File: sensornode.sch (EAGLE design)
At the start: 73 parts, among them IC1 CP2104, Q1 mmbt2222, Q2 mmbt2222, Q3 DMG3415U, SW2 KMR2, U1 TSL2591, U2 AP2112-3.3, U3 MCP73831T-2ACI/OT, U4 BMEx80, X2 ESP32_WROOM32_SKINNY, X4 20329

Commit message: Adding a 10uF Cap to the CP2104
This make it more closely resemble the known working designs.
Getting paranoid due to when this will need to get built.
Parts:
- added C5: 10uF, microbuilder:CAP_CERAMIC0805-NOOUTLINE
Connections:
- new net N$6: C5.2, IC1G$1.VDD
- net GND: now also C5.1
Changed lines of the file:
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@@
 <part name="U$31" library="microbuilder" deviceset="GND" device=""/>
 <part name="U$45" library="microbuilder" deviceset="3.3V" device=""/>
+<part name="C5" library="microbuilder" deviceset="CAP_CERAMIC" device="0805-NOOUTLINE" value="10uF"/>
+<part name="U$46" library="microbuilder" deviceset="GND" device=""/>
 </parts>
 <sheets>
@@
 <instance part="U$31" gate="G$1" x="292.1" y="5.08"/>
 <instance part="U$45" gate="G$1" x="276.86" y="63.5"/>
+<instance part="C5" gate="G$1" x="177.8" y="248.92"/>
+<instance part="U$46" gate="G$1" x="177.8" y="259.08" rot="R180"/>
 </instances>
 <busses>
@@
 <junction x="292.1" y="48.26"/>
 </segment>
+<segment>
+<pinref part="C5" gate="G$1" pin="1"/>
+<pinref part="U$46" gate="G$1" pin="GND"/>
+<wire x1="177.8" y1="254" x2="177.8" y2="256.54" width="0.1524" layer="91"/>
+</segment>
 </net>
 <net name="TXLED" class="0">
@@
 </segment>
 </net>
+<net name="N$6" class="0">
+<segment>
+<pinref part="IC1" gate="G$1" pin="VDD"/>
+<pinref part="C5" gate="G$1" pin="2"/>
+<wire x1="195.58" y1="243.84" x2="177.8" y2="243.84" width="0.1524" layer="91"/>
+<wire x1="177.8" y1="243.84" x2="177.8" y2="246.38" width="0.1524" layer="91"/>
+</segment>
+</net>

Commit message: Cleaning up a bunch of stuff
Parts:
- added JP1: (no value), pinhead:PINHD-1X6
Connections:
- net GND: now also JP1.1
- net RXD0: now also JP1.5
- net TXD0: now also JP1.4
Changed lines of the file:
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@@
 <part name="C5" library="microbuilder" deviceset="CAP_CERAMIC" device="0805-NOOUTLINE" value="10uF"/>
 <part name="U$46" library="microbuilder" deviceset="GND" device=""/>
+<part name="JP1" library="pinhead" deviceset="PINHD-1X6" device=""/>
 </parts>
 <sheets>
@@
 <instance part="C5" gate="G$1" x="177.8" y="248.92"/>
 <instance part="U$46" gate="G$1" x="177.8" y="259.08" rot="R180"/>
+<instance part="JP1" gate="A" x="274.32" y="165.1"/>
 </instances>
 <busses>
@@
 <wire x1="177.8" y1="254" x2="177.8" y2="256.54" width="0.1524" layer="91"/>
 </segment>
+<segment>
+<pinref part="JP1" gate="A" pin="1"/>
+<wire x1="271.78" y1="172.72" x2="254" y2="172.72" width="0.1524" layer="91"/>
+<label x="256.54" y="172.72" size="1.778" layer="95"/>
+</segment>
 </net>
 <net name="TXLED" class="0">
@@
 <label x="228.6" y="210.82" size="1.778" layer="95"/>
 </segment>
+<segment>
+<pinref part="JP1" gate="A" pin="5"/>
+<wire x1="271.78" y1="162.56" x2="254" y2="162.56" width="0.1524" layer="91"/>
+<label x="256.54" y="162.56" size="1.778" layer="95"/>
+</segment>
 </net>
 <net name="TXD0" class="0">
@@
 <label x="228.6" y="208.28" size="1.778" layer="95"/>
 </segment>
-</net>
+<segment>
+<pinref part="JP1" gate="A" pin="4"/>
+<wire x1="271.78" y1="165.1" x2="254" y2="165.1" width="0.1524" layer="91"/>
+<label x="256.54" y="165.1" size="1.778" layer="95"/>
+</segment>
+</net>

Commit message: Final cleanups going to prototype v2
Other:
- note added: "BACKUP FTDI Port"
- note added: "E-Ink Screen Connector"
- note added: "Micro SD Card Cage"
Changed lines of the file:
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@@
 <wire x1="71.12" y1="50.8" x2="71.12" y2="124.46" width="0.1524" layer="94" style="shortdash"/>
 <wire x1="251.46" y1="187.96" x2="284.48" y2="187.96" width="0.1524" layer="94" style="shortdash"/>
-<wire x1="251.46" y1="63.5" x2="251.46" y2="144.78" width="0.1524" layer="94" style="shortdash"/>
+<wire x1="251.46" y1="63.5" x2="251.46" y2="71.12" width="0.1524" layer="94" style="shortdash"/>
+<wire x1="251.46" y1="71.12" x2="251.46" y2="144.78" width="0.1524" layer="94" style="shortdash"/>
 <wire x1="251.46" y1="144.78" x2="251.46" y2="187.96" width="0.1524" layer="94" style="shortdash"/>
 <wire x1="251.46" y1="63.5" x2="236.22" y2="63.5" width="0.1524" layer="94" style="shortdash"/>
@@
 <text x="289.56" y="147.32" size="1.778" layer="97">BME280 - Temp, Humidity, Pressure
 BME680 - Temp, Humidity, Pressure, Particle</text>
-<wire x1="284.48" y1="71.12" x2="284.48" y2="162.56" width="0.1524" layer="94" style="shortdash"/>
-<wire x1="401.32" y1="71.12" x2="284.48" y2="71.12" width="0.1524" layer="94" style="shortdash"/>
+<wire x1="284.48" y1="71.12" x2="284.48" y2="144.78" width="0.1524" layer="94" style="shortdash"/>
+<wire x1="284.48" y1="144.78" x2="284.48" y2="162.56" width="0.1524" layer="94" style="shortdash"/>
+<wire x1="401.32" y1="71.12" x2="299.72" y2="71.12" width="0.1524" layer="94" style="shortdash"/>
+<text x="254" y="182.88" size="1.778" layer="94">BACKUP FTDI Port</text>
+<text x="149.86" y="139.7" size="1.778" layer="94">E-Ink Screen Connector</text>
+<wire x1="299.72" y1="71.12" x2="284.48" y2="71.12" width="0.1524" layer="94" style="shortdash"/>
+<wire x1="251.46" y1="144.78" x2="284.48" y2="144.78" width="0.1524" layer="94" style="shortdash"/>
+<text x="254" y="68.58" size="1.778" layer="94">Micro SD Card Cage</text>
+<wire x1="251.46" y1="71.12" x2="284.48" y2="71.12" width="0.1524" layer="94" style="shortdash"/>
+<wire x1="299.72" y1="22.86" x2="299.72" y2="71.12" width="0.1524" layer="94" style="shortdash"/>
 </plain>
 <instances>

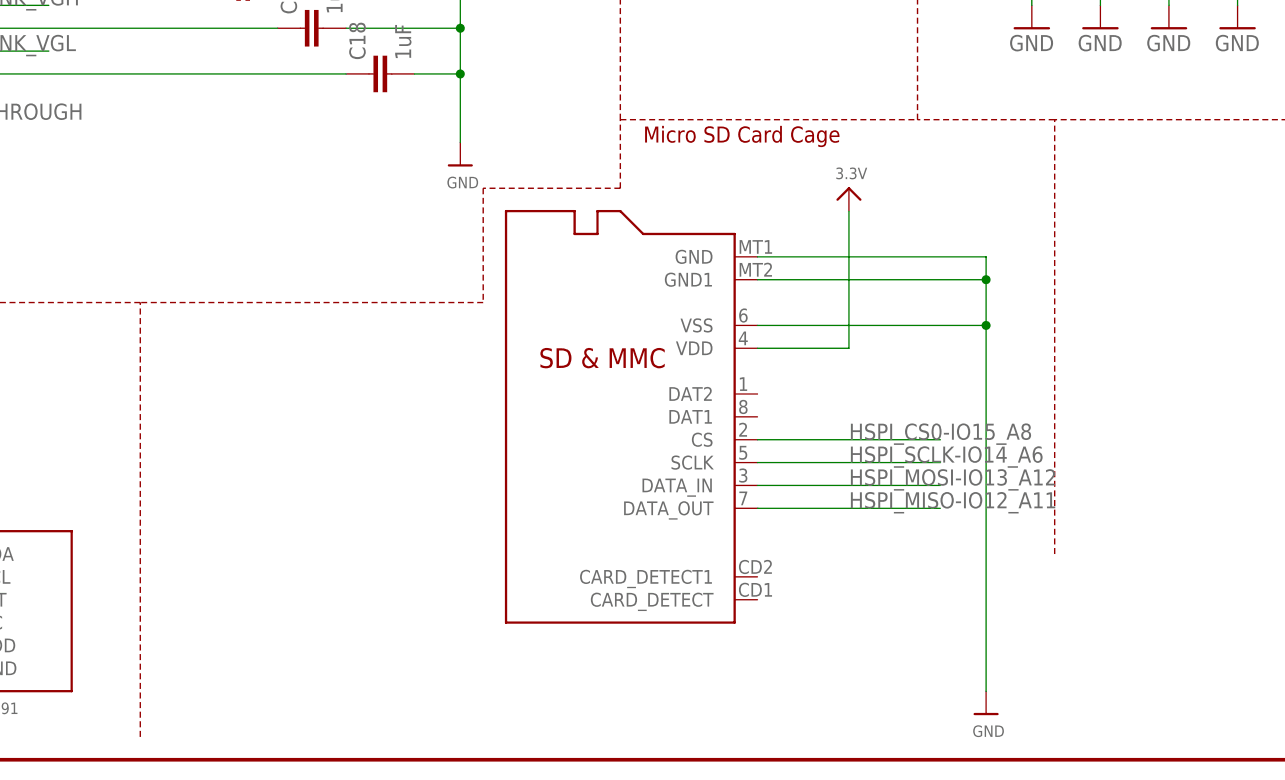
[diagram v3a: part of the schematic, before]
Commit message: Swapping out microSD cage for the Molex
The 4UConn cage is delightlyfully cheap, but the lead times are
dicey.  At least for this run I'm going to go with the easily
found, but more expensive, card cage, and I'll revert when
I've got more time on a different production run.
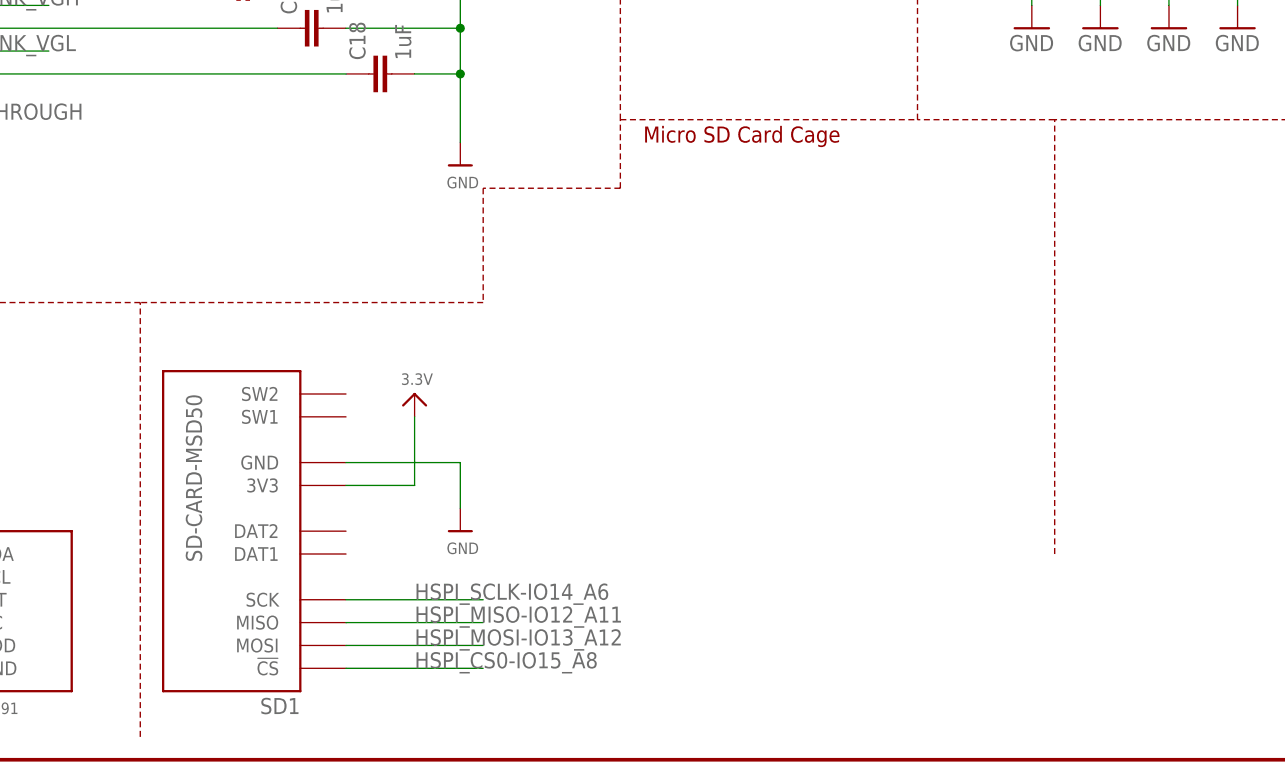
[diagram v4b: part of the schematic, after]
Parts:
- removed U$17: MICROSD, adafruit:MICROSD
- added SD1: SD-CARD-MSD50, we-con:SD-CARD-MSD50
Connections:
- net 3.3V: now also SD1.3V3; no longer U$17.VDD
- net GND: now also SD1.GND; no longer U$17.GND, U$17.GND1, U$17.VSS
- net HSPI_CS0-IO15_A8: now also SD1.!CS; no longer U$17.CS
- net HSPI_MISO-IO12_A11: now also SD1.MISO; no longer U$17.DATA_OUT
- net HSPI_MOSI-IO13_A12: now also SD1.MOSI; no longer U$17.DATA_IN
- net HSPI_SCLK-IO14_A6: now also SD1.SCK; no longer U$17.SCLK
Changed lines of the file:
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@@
 <part name="U$47" library="microbuilder" deviceset="GND" device=""/>
 <part name="U$18" library="microbuilder" deviceset="VBUS" device=""/>
-<part name="U$17" library="adafruit" deviceset="MICROSD" device=""/>
-<part name="U$31" library="microbuilder" deviceset="GND" device=""/>
-<part name="U$45" library="microbuilder" deviceset="3.3V" device=""/>
 <part name="C5" library="microbuilder" deviceset="CAP_CERAMIC" device="0805-NOOUTLINE" value="10uF"/>
 <part name="U$46" library="microbuilder" deviceset="GND" device=""/>
 <part name="JP1" library="pinhead" deviceset="PINHD-1X6" device=""/>
+<part name="SD1" library="we-con" deviceset="SD-CARD" device="-MSD50"/>
+<part name="U$48" library="microbuilder" deviceset="3.3V" device=""/>
+<part name="U$49" library="microbuilder" deviceset="GND" device=""/>
 </parts>
 <sheets>
@@
 <instance part="U$47" gate="G$1" x="177.8" y="226.06"/>
 <instance part="U$18" gate="G$1" x="167.64" y="259.08"/>
-<instance part="U$17" gate="G$1" x="248.92" y="35.56" rot="R180"/>
-<instance part="U$31" gate="G$1" x="292.1" y="5.08"/>
-<instance part="U$45" gate="G$1" x="276.86" y="63.5"/>
 <instance part="C5" gate="G$1" x="177.8" y="248.92"/>
 <instance part="U$46" gate="G$1" x="177.8" y="259.08" rot="R180"/>
 <instance part="JP1" gate="A" x="274.32" y="165.1"/>
+<instance part="SD1" gate="SD" x="208.28" y="25.4" rot="R180"/>
+<instance part="U$48" gate="G$1" x="228.6" y="40.64"/>
+<instance part="U$49" gate="G$1" x="233.68" y="25.4"/>
 </instances>
 <busses>
@@
 </segment>
 <segment>
-<pinref part="U$17" gate="G$1" pin="GND"/>
-<wire x1="266.7" y1="55.88" x2="292.1" y2="55.88" width="0.1524" layer="91"/>
-<wire x1="292.1" y1="55.88" x2="292.1" y2="53.34" width="0.1524" layer="91"/>
-<pinref part="U$31" gate="G$1" pin="GND"/>
-<pinref part="U$17" gate="G$1" pin="GND1"/>
-<wire x1="292.1" y1="53.34" x2="292.1" y2="48.26" width="0.1524" layer="91"/>
-<wire x1="292.1" y1="48.26" x2="292.1" y2="7.62" width="0.1524" layer="91"/>
-<wire x1="266.7" y1="53.34" x2="292.1" y2="53.34" width="0.1524" layer="91"/>
-<junction x="292.1" y="53.34"/>
-<pinref part="U$17" gate="G$1" pin="VSS"/>
-<wire x1="266.7" y1="48.26" x2="292.1" y2="48.26" width="0.1524" layer="91"/>
-<junction x="292.1" y="48.26"/>
-</segment>
-<segment>
 <pinref part="C5" gate="G$1" pin="1"/>
 <pinref part="U$46" gate="G$1" pin="GND"/>
@@
 <wire x1="271.78" y1="172.72" x2="254" y2="172.72" width="0.1524" layer="91"/>
 <label x="256.54" y="172.72" size="1.778" layer="95"/>
+</segment>
+<segment>
+<pinref part="SD1" gate="SD" pin="GND"/>
+<pinref part="U$49" gate="G$1" pin="GND"/>
+<wire x1="220.98" y1="33.02" x2="233.68" y2="33.02" width="0.1524" layer="91"/>
+<wire x1="233.68" y1="33.02" x2="233.68" y2="27.94" width="0.1524" layer="91"/>
 </segment>
 </net>
@@
 </segment>
 <segment>
-<pinref part="U$17" gate="G$1" pin="VDD"/>
-<pinref part="U$45" gate="G$1" pin="3.3V"/>
-<wire x1="266.7" y1="45.72" x2="276.86" y2="45.72" width="0.1524" layer="91"/>
-<wire x1="276.86" y1="45.72" x2="276.86" y2="60.96" width="0.1524" layer="91"/>
+<pinref part="SD1" gate="SD" pin="3V3"/>
+<pinref part="U$48" gate="G$1" pin="3.3V"/>
+<wire x1="220.98" y1="30.48" x2="228.6" y2="30.48" width="0.1524" layer="91"/>
+<wire x1="228.6" y1="30.48" x2="228.6" y2="38.1" width="0.1524" layer="91"/>
 </segment>
 </net>
@@
 </segment>
 <segment>
-<pinref part="U$17" gate="G$1" pin="DATA_IN"/>
-<wire x1="266.7" y1="30.48" x2="287.02" y2="30.48" width="0.1524" layer="91"/>
-<label x="276.86" y="30.48" size="1.778" layer="95"/>
+<pinref part="SD1" gate="SD" pin="MOSI"/>
+<wire x1="220.98" y1="12.7" x2="236.22" y2="12.7" width="0.1524" layer="91"/>
+<label x="228.6" y="12.7" size="1.778" layer="95"/>
 </segment>
 </net>
@@
 </segment>
 <segment>
-<pinref part="U$17" gate="G$1" pin="DATA_OUT"/>
-<wire x1="266.7" y1="27.94" x2="287.02" y2="27.94" width="0.1524" layer="91"/>
-<label x="276.86" y="27.94" size="1.778" layer="95"/>
+<pinref part="SD1" gate="SD" pin="MISO"/>
+<wire x1="220.98" y1="15.24" x2="236.22" y2="15.24" width="0.1524" layer="91"/>
+<label x="228.6" y="15.24" size="1.778" layer="95"/>
 </segment>
 </net>
@@
 </segment>
 <segment>
-<pinref part="U$17" gate="G$1" pin="CS"/>
-<wire x1="266.7" y1="35.56" x2="287.02" y2="35.56" width="0.1524" layer="91"/>
-<label x="276.86" y="35.56" size="1.778" layer="95"/>
+<pinref part="SD1" gate="SD" pin="!CS"/>
+<wire x1="220.98" y1="10.16" x2="236.22" y2="10.16" width="0.1524" layer="91"/>
+<label x="228.6" y="10.16" size="1.778" layer="95"/>
 </segment>
 </net>
@@
 </segment>
 <segment>
-<pinref part="U$17" gate="G$1" pin="SCLK"/>
-<wire x1="266.7" y1="33.02" x2="287.02" y2="33.02" width="0.1524" layer="91"/>
-<label x="276.86" y="33.02" size="1.778" layer="95"/>
-</segment>
-</net>
+<pinref part="SD1" gate="SD" pin="SCK"/>
+<wire x1="220.98" y1="17.78" x2="236.22" y2="17.78" width="0.1524" layer="91"/>
+<label x="228.6" y="17.78" size="1.778" layer="95"/>
+</segment>
+</net>

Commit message: Adjusting e-ink screen, and reving to v1.2
So this adds C22, a 1uF cap on VGL and R20 to EINK_GDR.  These
fall in line with what's on the waveshare and Open Hardware Summit
badge and should be slightly more reliable than my current circuit
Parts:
- added C22: 1uF, SparkFun-Capacitors:0.1UF-25V-5%(0603)
- added R20: 10K, SparkFun-Resistors:4.7KOHM-1/10W-1%(0603)
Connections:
- new net N$24: C22.1, U$15.4-NC2
- net EINK_GDR: now also R20.1
- net GND: now also C22.2, R20.2
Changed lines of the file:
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@@
 <part name="U$48" library="microbuilder" deviceset="3.3V" device=""/>
 <part name="U$49" library="microbuilder" deviceset="GND" device=""/>
+<part name="R20" library="SparkFun-Resistors" deviceset="4.7KOHM-1/10W-1%(0603)" device="" value="10K"/>
+<part name="C22" library="SparkFun-Capacitors" deviceset="0.1UF-25V-5%(0603)" device="" value="1uF"/>
 </parts>
 <sheets>
@@
 <instance part="U$48" gate="G$1" x="228.6" y="40.64"/>
 <instance part="U$49" gate="G$1" x="233.68" y="25.4"/>
+<instance part="R20" gate="G$1" x="198.12" y="137.16"/>
+<instance part="C22" gate="G$1" x="205.74" y="127" rot="R90"/>
 </instances>
 <busses>
@@
 <wire x1="228.6" y1="76.2" x2="233.68" y2="76.2" width="0.1524" layer="91"/>
 <junction x="233.68" y="76.2"/>
+<pinref part="R20" gate="G$1" pin="2"/>
+<wire x1="203.2" y1="137.16" x2="233.68" y2="137.16" width="0.1524" layer="91"/>
+<wire x1="233.68" y1="137.16" x2="233.68" y2="127" width="0.1524" layer="91"/>
+<junction x="233.68" y="124.46"/>
+<pinref part="C22" gate="G$1" pin="2"/>
+<wire x1="233.68" y1="127" x2="233.68" y2="124.46" width="0.1524" layer="91"/>
+<wire x1="208.28" y1="127" x2="233.68" y2="127" width="0.1524" layer="91"/>
+<junction x="233.68" y="127"/>
 </segment>
 <segment>
@@
 <segment>
 <pinref part="U$15" gate="G$1" pin="2-GDR"/>
-<wire x1="162.56" y1="132.08" x2="187.96" y2="132.08" width="0.1524" layer="91"/>
+<wire x1="162.56" y1="132.08" x2="177.8" y2="132.08" width="0.1524" layer="91"/>
 <label x="180.34" y="132.08" size="1.778" layer="95"/>
+<pinref part="R20" gate="G$1" pin="1"/>
+<wire x1="177.8" y1="132.08" x2="187.96" y2="132.08" width="0.1524" layer="91"/>
+<wire x1="177.8" y1="132.08" x2="177.8" y2="137.16" width="0.1524" layer="91"/>
+<wire x1="177.8" y1="137.16" x2="193.04" y2="137.16" width="0.1524" layer="91"/>
+<junction x="177.8" y="132.08"/>
 </segment>
 </net>
@@
 </segment>
 </net>
+<net name="N$24" class="0">
+<segment>
+<pinref part="U$15" gate="G$1" pin="4-NC2"/>
+<pinref part="C22" gate="G$1" pin="1"/>
+<wire x1="162.56" y1="127" x2="200.66" y2="127" width="0.1524" layer="91"/>
+</segment>
+</net>

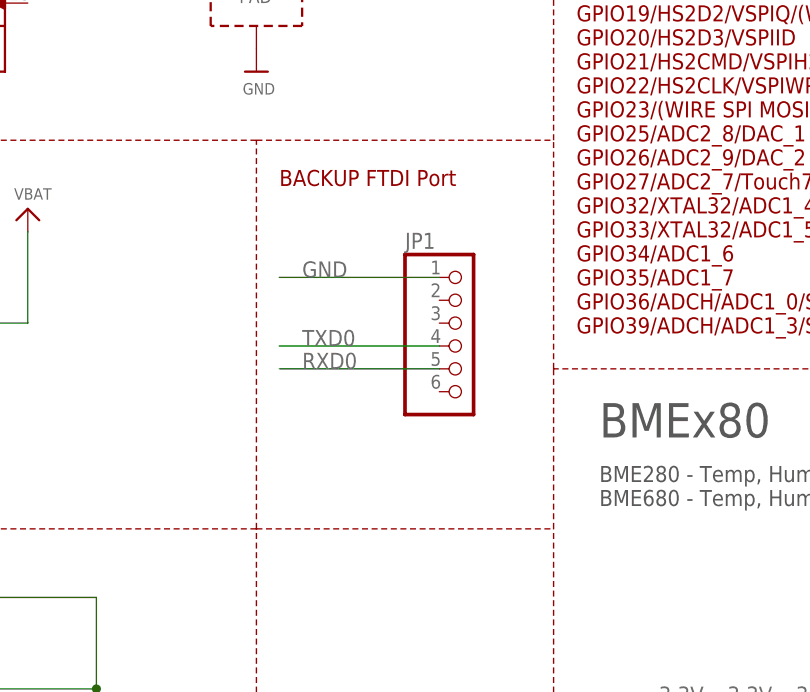
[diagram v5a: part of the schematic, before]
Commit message: Removing the backup FTDI port
As it turns out my luck with the power changes to the serial port
chip worked just fine, and as a result the FTDI header is actually
extraneous and obnoxious.  Remove it, get the board a little
smaller.
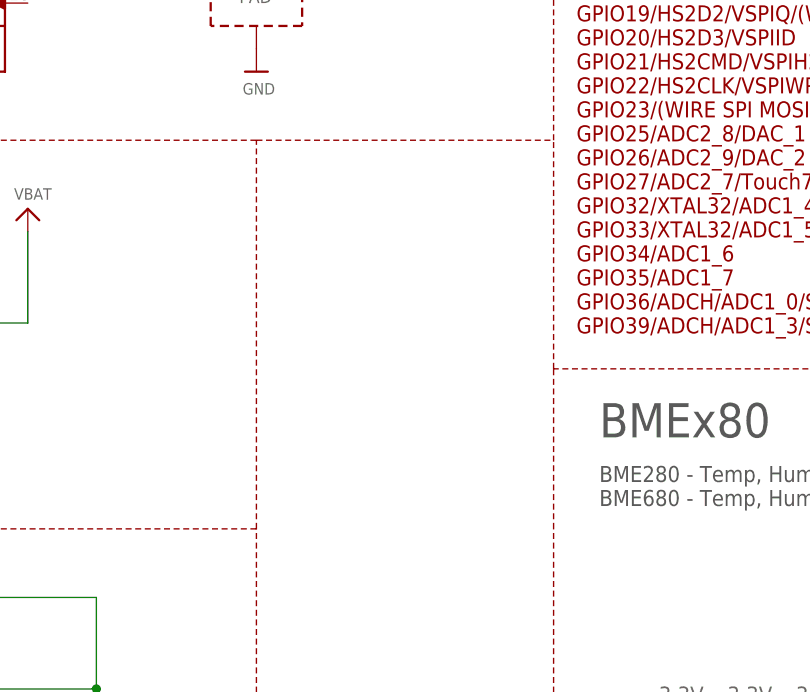
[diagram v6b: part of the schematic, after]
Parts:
- removed JP1: (no value), pinhead:PINHD-1X6
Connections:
- net GND: no longer JP1.1
- net RXD0: no longer JP1.5
- net TXD0: no longer JP1.4
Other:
- note removed: "BACKUP FTDI Port"
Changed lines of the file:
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@@
 <part name="C5" library="microbuilder" deviceset="CAP_CERAMIC" device="0805-NOOUTLINE" value="10uF"/>
 <part name="U$46" library="microbuilder" deviceset="GND" device=""/>
-<part name="JP1" library="pinhead" deviceset="PINHD-1X6" device=""/>
 <part name="SD1" library="we-con" deviceset="SD-CARD" device="-MSD50"/>
 <part name="U$48" library="microbuilder" deviceset="3.3V" device=""/>
@@
 <wire x1="284.48" y1="144.78" x2="284.48" y2="162.56" width="0.1524" layer="94" style="shortdash"/>
 <wire x1="401.32" y1="71.12" x2="299.72" y2="71.12" width="0.1524" layer="94" style="shortdash"/>
-<text x="254" y="182.88" size="1.778" layer="94">BACKUP FTDI Port</text>
 <text x="149.86" y="139.7" size="1.778" layer="94">E-Ink Screen Connector</text>
 <wire x1="299.72" y1="71.12" x2="284.48" y2="71.12" width="0.1524" layer="94" style="shortdash"/>
-<wire x1="251.46" y1="144.78" x2="284.48" y2="144.78" width="0.1524" layer="94" style="shortdash"/>
 <text x="254" y="68.58" size="1.778" layer="94">Micro SD Card Cage</text>
 <wire x1="251.46" y1="71.12" x2="284.48" y2="71.12" width="0.1524" layer="94" style="shortdash"/>
@@
 <instance part="C5" gate="G$1" x="177.8" y="248.92"/>
 <instance part="U$46" gate="G$1" x="177.8" y="259.08" rot="R180"/>
-<instance part="JP1" gate="A" x="274.32" y="165.1"/>
 <instance part="SD1" gate="SD" x="208.28" y="25.4" rot="R180"/>
 <instance part="U$48" gate="G$1" x="228.6" y="40.64"/>
@@
 </segment>
 <segment>
-<pinref part="JP1" gate="A" pin="1"/>
-<wire x1="271.78" y1="172.72" x2="254" y2="172.72" width="0.1524" layer="91"/>
-<label x="256.54" y="172.72" size="1.778" layer="95"/>
-</segment>
-<segment>
 <pinref part="SD1" gate="SD" pin="GND"/>
 <pinref part="U$49" gate="G$1" pin="GND"/>
@@
 <label x="228.6" y="210.82" size="1.778" layer="95"/>
 </segment>
-<segment>
-<pinref part="JP1" gate="A" pin="5"/>
-<wire x1="271.78" y1="162.56" x2="254" y2="162.56" width="0.1524" layer="91"/>
-<label x="256.54" y="162.56" size="1.778" layer="95"/>
-</segment>
 </net>
 <net name="TXD0" class="0">
@@
 <label x="228.6" y="208.28" size="1.778" layer="95"/>
 </segment>
-<segment>
-<pinref part="JP1" gate="A" pin="4"/>
-<wire x1="271.78" y1="165.1" x2="254" y2="165.1" width="0.1524" layer="91"/>
-<label x="256.54" y="165.1" size="1.778" layer="95"/>
-</segment>
-</net>
+</net>
